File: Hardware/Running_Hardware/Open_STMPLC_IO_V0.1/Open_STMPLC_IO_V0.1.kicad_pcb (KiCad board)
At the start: 4 copper layers, 168.8 x 90 mm, 555 parts, among them J1 Screw_Terminal_01x10, J2 Screw_Terminal_01x06, J3 Screw_Terminal_01x04, J33 Screw_Terminal_01x02, J34 Screw_Terminal_01x02, J35 Screw_Terminal_01x03, J36 Screw_Terminal_01x03, J37 Screw_Terminal_01x03, J38 Screw_Terminal_01x03, J39 10144517-041802LF, J4 Screw_Terminal_01x02, J40 Screw_Terminal_01x04, J41 10144517-041802LF, J42 10144517-041802LF, J43 Screw_Terminal_01x02, J5 Screw_Terminal_01x04, J6 Screw_Terminal_01x04, J7 Screw_Terminal_01x04, J8 Screw_Terminal_01x04, J9 DE9_Pins, Q1 2N7002K, Q2 2N7002K, Q3 2N7002K, Q4 2N7002K, Q5 AOD407, Q6 AOD407, Q7 MMBT5401, U1 TPS1H200A, U10 MAX31865xTP, U11 MAX31856, U12 6N137, U13 TPS1H200A, U14 TPS26600PWP, U15 NVTFS5124PLTAG, U16 TPS26600PWP, U17 NVTFS5124PLTAG, U18 TPS26600PWP, U19 NVTFS5124PLTAG, U2 TPS1H200A, U20 6N137, U21 6N137, U22 6N137, U23 6N137, U24 6N137, U25 6N137, U26 6N137, U27 6N137, U28 6N137, U29 6N137, U3 TPS1H200A, U30 6N137, U37 XTR305, U38 XTR305, U39 AD4111, U4 TPS1H200A, U40 REF3025, U41 MAX31865xTP, U5 TPS1H200A, U6 TPS1H200A, U7 TPS26600PWP, U8 NVTFS5124PLTAG, U9 TPS1H200A, Y2 16MHz

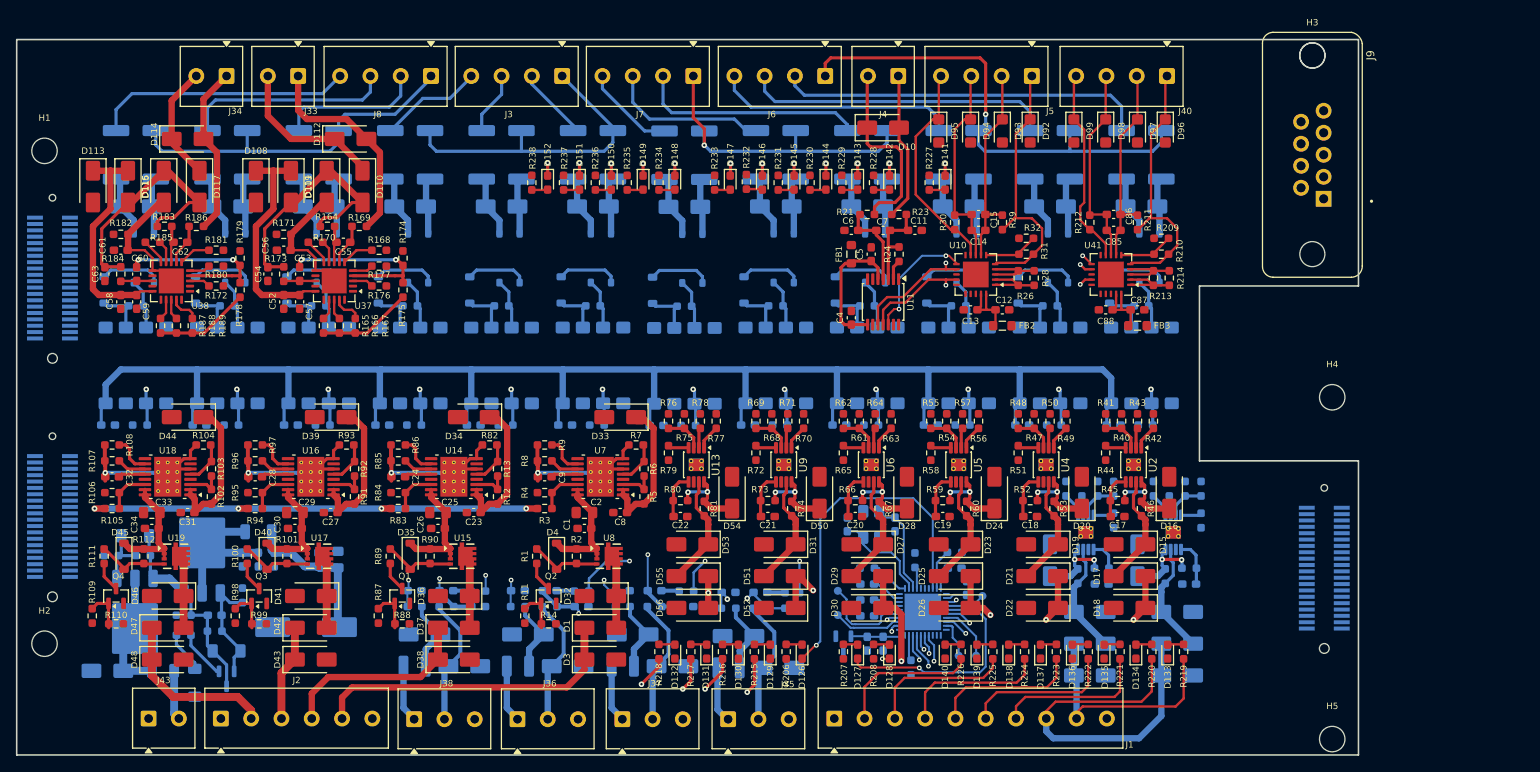
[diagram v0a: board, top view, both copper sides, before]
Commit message: Pin mapping IO connector
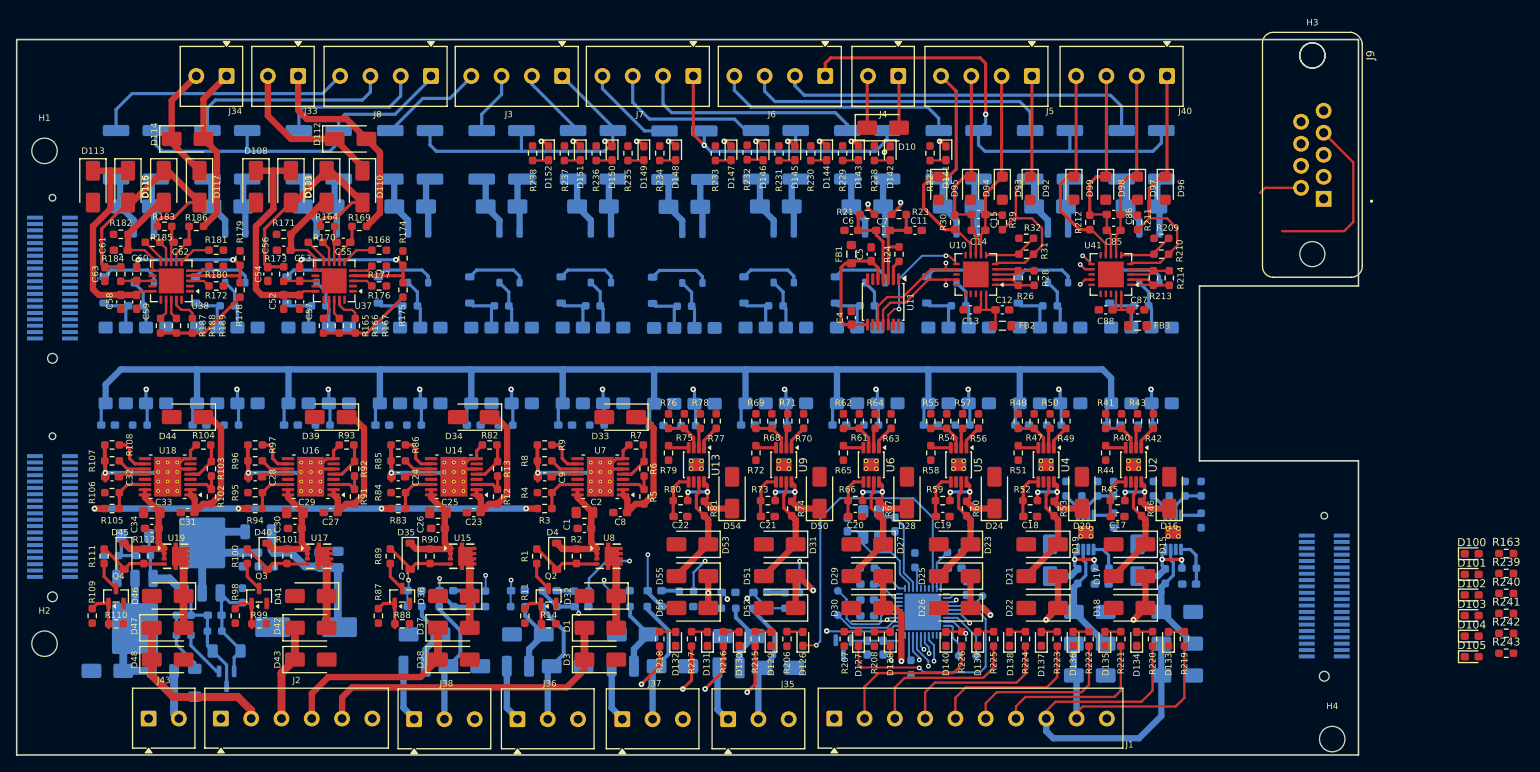
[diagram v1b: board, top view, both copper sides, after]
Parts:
- removed H5: MountingHole, MountingHole:MountingHole_3.2mm_M3
- added D100: LED, LED_SMD:LED_0603_1608Metric_Pad1.05x0.95mm_HandSolder, F.Cu at (231.0, 124.7)
- added D101: LED, LED_SMD:LED_0603_1608Metric_Pad1.05x0.95mm_HandSolder, F.Cu at (231.0, 127.3)
- added D102: LED, LED_SMD:LED_0603_1608Metric_Pad1.05x0.95mm_HandSolder, F.Cu at (231.0, 129.9)
- added D103: LED, LED_SMD:LED_0603_1608Metric_Pad1.05x0.95mm_HandSolder, F.Cu at (231.0, 132.5)
- added D104: LED, LED_SMD:LED_0603_1608Metric_Pad1.05x0.95mm_HandSolder, F.Cu at (231.0, 135.1)
- added D105: LED, LED_SMD:LED_0603_1608Metric_Pad1.05x0.95mm_HandSolder, F.Cu at (231.0, 137.6)
- added R163: 470R, Resistor_SMD:R_0603_1608Metric_Pad0.98x0.95mm_HandSolder, F.Cu at (235.4, 124.7)
- added R239: 470R, Resistor_SMD:R_0603_1608Metric_Pad0.98x0.95mm_HandSolder, F.Cu at (235.4, 127.2)
- added R240: 470R, Resistor_SMD:R_0603_1608Metric_Pad0.98x0.95mm_HandSolder, F.Cu at (235.4, 129.7)
- added R241: 470R, Resistor_SMD:R_0603_1608Metric_Pad0.98x0.95mm_HandSolder, F.Cu at (235.4, 132.2)
- added R242: 470R, Resistor_SMD:R_0603_1608Metric_Pad0.98x0.95mm_HandSolder, F.Cu at (235.4, 134.7)
- added R243: 470R, Resistor_SMD:R_0603_1608Metric_Pad0.98x0.95mm_HandSolder, F.Cu at (235.4, 137.2)
- moved H4 43.0 mm to (213.5, 148.0)
- moved D92 7.20 mm to (175.5, 78.7)
- moved D93 7.20 mm to (172.0, 78.7)
- moved D94 7.20 mm to (168.0, 78.7)
- moved D95 7.20 mm to (164.0, 78.7)
- moved D96 7.20 mm to (192.5, 78.7)
- moved D97 7.20 mm to (189.0, 78.7)
- moved D98 7.20 mm to (185.0, 78.7)
- moved D99 7.20 mm to (181.0, 78.7)
- moved D147 3.70 mm to (137.9, 74.3)
- moved D141 3.70 mm to (164.9, 74.3)
- moved D142 3.70 mm to (157.9, 74.3)
- moved D143 3.70 mm to (153.9, 74.3)
- moved D144 3.70 mm to (149.9, 74.3)
- moved D145 3.70 mm to (145.9, 74.3)
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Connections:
- J39 pad 1: unconnected-(J39-Pin_1-Pad1) -> GND
- J39 pad 2: unconnected-(J39-Pin_2-Pad2) -> GND
- J39 pad 39: unconnected-(J39-Pin_39-Pad39) -> GND
- J39 pad 40: unconnected-(J39-Pin_40-Pad40) -> GND
- J41 pad 1: unconnected-(J41-Pin_1-Pad1) -> GND
- J41 pad 2: unconnected-(J41-Pin_2-Pad2) -> GND
- J41 pad 3: unconnected-(J41-Pin_3-Pad3) -> +24V
- J41 pad 39: unconnected-(J41-Pin_39-Pad39) -> GND
- J41 pad 4: unconnected-(J41-Pin_4-Pad4) -> +3V3
- J41 pad 40: unconnected-(J41-Pin_40-Pad40) -> GND
- J41 pad 5: unconnected-(J41-Pin_5-Pad5) -> +24V
- J41 pad 6: unconnected-(J41-Pin_6-Pad6) -> +3V3
- J41 pad 7: unconnected-(J41-Pin_7-Pad7) -> +24V
- J41 pad 8: unconnected-(J41-Pin_8-Pad8) -> +3V3
- J42 pad 1: unconnected-(J42-Pin_1-Pad1) -> GND
- J42 pad 2: unconnected-(J42-Pin_2-Pad2) -> GND
- J42 pad 33: unconnected-(J42-Pin_33-Pad33) -> /B2B_Connector/AB-
- J42 pad 34: unconnected-(J42-Pin_34-Pad34) -> /B2B_Connector/YZ+
- J42 pad 35: unconnected-(J42-Pin_35-Pad35) -> /B2B_Connector/AB+
- J42 pad 36: unconnected-(J42-Pin_36-Pad36) -> /B2B_Connector/YZ-
- J42 pad 37: unconnected-(J42-Pin_37-Pad37) -> /B2B_Connector/3V3_ISO
- J42 pad 38: unconnected-(J42-Pin_38-Pad38) -> GND_MODBUS
- J42 pad 39: unconnected-(J42-Pin_39-Pad39) -> GND
- J42 pad 40: unconnected-(J42-Pin_40-Pad40) -> GND
- J9 pad 1: unconnected-(J9-Pad1) -> GND_MODBUS
- J9 pad 2: unconnected-(J9-Pad2) -> /B2B_Connector/AB-
- J9 pad 3: unconnected-(J9-Pad3) -> /B2B_Connector/AB+
- J9 pad 4: unconnected-(J9-Pad4) -> /B2B_Connector/YZ-
- J9 pad 5: unconnected-(J9-Pad5) -> GND_MODBUS
- J9 pad 6: unconnected-(J9-Pad6) -> /B2B_Connector/YZ+
- J9 pad 9: unconnected-(J9-Pad9) -> /B2B_Connector/3V3_ISO
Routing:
- net /B2B_Connector/YZ-: track 0.00 -> 22.2 mm
- net Net-(D10-A2): track 18.7 -> 24.5 mm, vias 0 -> 1
- net /B2B_Connector/YZ+: track 0.00 -> 5.45 mm
- net /B2B_Connector/DIG_IN_4: track 40.0 -> 42.8 mm
- net /B2B_Connector/DIG_IN_3: track 46.9 -> 49.7 mm
- net Net-(D91-K): track 5.20 -> 7.71 mm
- net /ANALOG_IN/VIN2: track 50.6 -> 53.1 mm
- net /B2B_Connector/DIG_IN_1: track 61.6 -> 63.9 mm
- net Net-(D99-A1): track 24.9 -> 27.0 mm
- net /B2B_Connector/DIG_IN_5: track 35.0 -> 37.1 mm
- net Net-(D95-A1): track 27.6 -> 29.5 mm
- net /B2B_Connector/DIG_OUT_TERMINAL_7: track 72.3 -> 73.9 mm
- net /B2B_Connector/DIG_OUT_TERMINAL_5: track 40.5 -> 42.1 mm
- net /B2B_Connector/DIG_OUT_TERMINAL_3: track 46.9 -> 48.5 mm
- net /B2B_Connector/DIG_OUT_TERMINAL_2: track 46.0 -> 47.7 mm
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
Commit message: IO board layout
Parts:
- moved R243 81.9 mm to (183.0, 74.3), turned to 90 degrees
- moved D105 78.4 mm to (184.9, 74.3), turned to -90 degrees
- moved R242 77.4 mm to (186.9, 74.3), turned to 90 degrees
- moved D104 73.9 mm to (188.9, 74.3), turned to -90 degrees
- moved R241 72.9 mm to (191.0, 74.3), turned to 90 degrees
- moved D103 69.6 mm to (192.9, 74.3), turned to -90 degrees
- moved R240 32.0 mm to (205.9, 142.0)
- moved R239 31.1 mm to (205.9, 136.9)
- moved R163 30.4 mm to (205.9, 132.0)
- moved D102 27.1 mm to (205.9, 139.9), turned to 180 degrees
- moved D101 26.2 mm to (205.9, 134.8), turned to 180 degrees
- moved D100 25.7 mm to (205.9, 129.9), turned to 180 degrees
- moved C83 2.83 mm to (150.5, 123.0), turned to -90 degrees
- moved Y2 2.24 mm to (154.5, 123.0), turned to 180 degrees
- moved C84 2.00 mm to (158.5, 123.0), turned to 90 degrees
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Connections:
- D100 pad 1: /B2B_Connector/POWER_LED -> GND
- D103 pad 1: /B2B_Connector/Ethernet_Link_LED -> /B2B_Connector/NET_STATUS_LED
- D104 pad 1: /B2B_Connector/Ethernet_Activity_LED -> /B2B_Connector/NET_MODE_LED
- D105 pad 1: /B2B_Connector/Internet_Status_LED -> /B2B_Connector/GSM_STATUS_LED
- J39 pad 10: unconnected-(J39-Pin_10-Pad10) -> /ANALOG_OUT/AOUT_~{OD}_2
- J39 pad 11: unconnected-(J39-Pin_11-Pad11) -> /ANALOG_OUT/AOUT_EFOT_1
- J39 pad 12: unconnected-(J39-Pin_12-Pad12) -> /ANALOG_OUT/AOUT_EFOT_2
- J39 pad 13: unconnected-(J39-Pin_13-Pad13) -> /ANALOG_OUT/AOUT_EFLD_1
- J39 pad 14: unconnected-(J39-Pin_14-Pad14) -> /ANALOG_OUT/AOUT_EFLD_2
- J39 pad 15: unconnected-(J39-Pin_15-Pad15) -> /ANALOG_OUT/AOUT_EFCM_1
- J39 pad 16: unconnected-(J39-Pin_16-Pad16) -> /ANALOG_OUT/AOUT_EFCM_2
- J39 pad 17: unconnected-(J39-Pin_17-Pad17) -> /B2B_Connector/TEMP_MISO
- J39 pad 18: unconnected-(J39-Pin_18-Pad18) -> /B2B_Connector/THRM_~{CS}
- J39 pad 19: unconnected-(J39-Pin_19-Pad19) -> /B2B_Connector/RTD_~{CS}_1
- J39 pad 20: unconnected-(J39-Pin_20-Pad20) -> /B2B_Connector/THRM_~{FAULT}
- J39 pad 21: unconnected-(J39-Pin_21-Pad21) -> /B2B_Connector/RTD_~{CS}_2
- J39 pad 22: unconnected-(J39-Pin_22-Pad22) -> /B2B_Connector/RTD_~{DRDY}_1
- J39 pad 23: unconnected-(J39-Pin_23-Pad23) -> /B2B_Connector/TEMP_SCLK
- J39 pad 24: unconnected-(J39-Pin_24-Pad24) -> /B2B_Connector/THRM_~{DRDY}
- J39 pad 25: unconnected-(J39-Pin_25-Pad25) -> /B2B_Connector/TEMP_MOSI
- J39 pad 26: unconnected-(J39-Pin_26-Pad26) -> /B2B_Connector/RTD_~{DRDY}_2
- J39 pad 27: unconnected-(J39-Pin_27-Pad27) -> /B2B_Connector/DIG_IN_6
- J39 pad 28: unconnected-(J39-Pin_28-Pad28) -> /B2B_Connector/GSM_STATUS_LED
- J39 pad 29: unconnected-(J39-Pin_29-Pad29) -> /B2B_Connector/DIG_IN_5
- J39 pad 3: unconnected-(J39-Pin_3-Pad3) -> /ANALOG_OUT/AOUT_VIN_1
- J39 pad 30: unconnected-(J39-Pin_30-Pad30) -> /B2B_Connector/NET_MODE_LED
- J39 pad 31: unconnected-(J39-Pin_31-Pad31) -> /B2B_Connector/DIG_IN_4
- J39 pad 32: unconnected-(J39-Pin_32-Pad32) -> /B2B_Connector/NET_STATUS_LED
- J39 pad 33: unconnected-(J39-Pin_33-Pad33) -> /B2B_Connector/DIG_IN_3
- J39 pad 35: unconnected-(J39-Pin_35-Pad35) -> /B2B_Connector/DIG_IN_2
- J39 pad 37: unconnected-(J39-Pin_37-Pad37) -> /B2B_Connector/DIG_IN_1
- J39 pad 4: unconnected-(J39-Pin_4-Pad4) -> /ANALOG_OUT/AOUT_VIN_2
- J39 pad 5: unconnected-(J39-Pin_5-Pad5) -> /ANALOG_OUT/AOUT_M1_1
- J39 pad 6: unconnected-(J39-Pin_6-Pad6) -> /ANALOG_OUT/AOUT_M1_2
- J39 pad 7: unconnected-(J39-Pin_7-Pad7) -> /ANALOG_OUT/AOUT_M2_1
- J39 pad 8: unconnected-(J39-Pin_8-Pad8) -> /ANALOG_OUT/AOUT_M2_2
- J39 pad 9: unconnected-(J39-Pin_9-Pad9) -> /ANALOG_OUT/AOUT_~{OD}_1
- J41 pad 10: unconnected-(J41-Pin_10-Pad10) -> /B2B_Connector/DIG_HS_IMON_2
- J41 pad 11: unconnected-(J41-Pin_11-Pad11) -> /B2B_Connector/DIG_HS_~{FAULT}_1
- J41 pad 12: unconnected-(J41-Pin_12-Pad12) -> /B2B_Connector/DIG_HS_~{FAULT}_2
- J41 pad 13: unconnected-(J41-Pin_13-Pad13) -> /B2B_Connector/DIG_HS_OUT_1
- J41 pad 14: unconnected-(J41-Pin_14-Pad14) -> /B2B_Connector/DIG_HS_OUT_2
- J41 pad 15: unconnected-(J41-Pin_15-Pad15) -> GND
- J41 pad 16: unconnected-(J41-Pin_16-Pad16) -> GND
- J41 pad 17: unconnected-(J41-Pin_17-Pad17) -> /B2B_Connector/DIG_HS_OUT_3
- J41 pad 18: unconnected-(J41-Pin_18-Pad18) -> /B2B_Connector/DIG_HS_OUT_4
- J41 pad 19: unconnected-(J41-Pin_19-Pad19) -> /B2B_Connector/DIG_HS_~{SHDN}_3
- J41 pad 20: unconnected-(J41-Pin_20-Pad20) -> /B2B_Connector/DIG_HS_~{SHDN}_4
- J41 pad 21: unconnected-(J41-Pin_21-Pad21) -> /B2B_Connector/DIG_HS_~{FAULT}_3
- J41 pad 22: unconnected-(J41-Pin_22-Pad22) -> /B2B_Connector/DIG_HS_IMON_4
- J41 pad 23: unconnected-(J41-Pin_23-Pad23) -> /B2B_Connector/DIG_HS_IMON_3
- J41 pad 24: unconnected-(J41-Pin_24-Pad24) -> /B2B_Connector/DIG_HS_~{FAULT}_4
- J41 pad 25: unconnected-(J41-Pin_25-Pad25) -> GND
- J41 pad 26: unconnected-(J41-Pin_26-Pad26) -> GND
- J41 pad 27: unconnected-(J41-Pin_27-Pad27) -> /ANALOG_IN/ANALOG_IN_DOUT
- J41 pad 28: unconnected-(J41-Pin_28-Pad28) -> /ANALOG_IN/ANALOG_IN_CS
- J41 pad 29: unconnected-(J41-Pin_29-Pad29) -> /ANALOG_IN/ANALOG_IN_DIN
- J41 pad 30: unconnected-(J41-Pin_30-Pad30) -> /ANALOG_IN/ANALOG_IN_ERROR
- J41 pad 31: unconnected-(J41-Pin_31-Pad31) -> /ANALOG_IN/ANALOG_IN_SCLK
- J41 pad 32: unconnected-(J41-Pin_32-Pad32) -> GND
- J41 pad 33: unconnected-(J41-Pin_33-Pad33) -> /B2B_Connector/DIG_IN_10
- J41 pad 34: unconnected-(J41-Pin_34-Pad34) -> /B2B_Connector/DIG_IN_7
- J41 pad 35: unconnected-(J41-Pin_35-Pad35) -> /B2B_Connector/DIG_IN_11
- J41 pad 36: unconnected-(J41-Pin_36-Pad36) -> /B2B_Connector/DIG_IN_8
- J41 pad 37: unconnected-(J41-Pin_37-Pad37) -> /B2B_Connector/DIG_IN_12
- J41 pad 38: unconnected-(J41-Pin_38-Pad38) -> /B2B_Connector/DIG_IN_9
- J41 pad 7: +24V -> /B2B_Connector/DIG_HS_~{SHDN}_1
- J41 pad 8: +3V3 -> /B2B_Connector/DIG_HS_~{SHDN}_2
- J41 pad 9: unconnected-(J41-Pin_9-Pad9) -> /B2B_Connector/DIG_HS_IMON_1
- J42 pad 10: unconnected-(J42-Pin_10-Pad10) -> /B2B_Connector/DIG_OUT_~{FAULT}_5
- J42 pad 11: unconnected-(J42-Pin_11-Pad11) -> /B2B_Connector/DIG_OUT_DIAG_6
- J42 pad 12: unconnected-(J42-Pin_12-Pad12) -> /B2B_Connector/DIG_OUT_DIAG_5
- J42 pad 13: unconnected-(J42-Pin_13-Pad13) -> /B2B_Connector/DIG_OUT_6
- J42 pad 14: unconnected-(J42-Pin_14-Pad14) -> /B2B_Connector/DIG_OUT_5
- J42 pad 15: unconnected-(J42-Pin_15-Pad15) -> /B2B_Connector/RUN_LED
- J42 pad 16: unconnected-(J42-Pin_16-Pad16) -> /B2B_Connector/FAULT_LED
- J42 pad 17: unconnected-(J42-Pin_17-Pad17) -> /B2B_Connector/DIG_OUT_~{FAULT}_4
- J42 pad 18: unconnected-(J42-Pin_18-Pad18) -> /B2B_Connector/DIG_OUT_~{FAULT}_3
- J42 pad 19: unconnected-(J42-Pin_19-Pad19) -> /B2B_Connector/DIG_OUT_DIAG_4
- J42 pad 20: unconnected-(J42-Pin_20-Pad20) -> /B2B_Connector/DIG_OUT_DIAG_3
- J42 pad 21: unconnected-(J42-Pin_21-Pad21) -> /B2B_Connector/DIG_OUT_4
- J42 pad 22: unconnected-(J42-Pin_22-Pad22) -> /B2B_Connector/DIG_OUT_3
- J42 pad 23: unconnected-(J42-Pin_23-Pad23) -> /B2B_Connector/DIG_OUT_2
- J42 pad 24: unconnected-(J42-Pin_24-Pad24) -> /B2B_Connector/DIG_OUT_1
- J42 pad 25: unconnected-(J42-Pin_25-Pad25) -> /B2B_Connector/DIG_OUT_DIAG_2
- J42 pad 26: unconnected-(J42-Pin_26-Pad26) -> /B2B_Connector/DIG_OUT_DIAG_1
- J42 pad 27: unconnected-(J42-Pin_27-Pad27) -> /B2B_Connector/DIG_OUT_~{FAULT}_2
- J42 pad 28: unconnected-(J42-Pin_28-Pad28) -> /B2B_Connector/DIG_OUT_~{FAULT}_1
- J42 pad 29: unconnected-(J42-Pin_29-Pad29) -> /B2B_Connector/3V3_ISO
- J42 pad 3: unconnected-(J42-Pin_3-Pad3) -> /B2B_Connector/DIG_OUT_~{FAULT}_7
- J42 pad 30: unconnected-(J42-Pin_30-Pad30) -> GND
- J42 pad 31: unconnected-(J42-Pin_31-Pad31) -> GND_MODBUS
- J42 pad 32: unconnected-(J42-Pin_32-Pad32) -> GND_MODBUS
- J42 pad 33: /B2B_Connector/AB- -> /B2B_Connector/YZ-
- J42 pad 34: /B2B_Connector/YZ+ -> /B2B_Connector/AB-
- J42 pad 35: /B2B_Connector/AB+ -> /B2B_Connector/YZ+
- J42 pad 36: /B2B_Connector/YZ- -> /B2B_Connector/AB+
- J42 pad 37: /B2B_Connector/3V3_ISO -> GND_MODBUS
- J42 pad 4: unconnected-(J42-Pin_4-Pad4) -> /B2B_Connector/DIG_OUT_~{FAULT}_8
- J42 pad 5: unconnected-(J42-Pin_5-Pad5) -> /B2B_Connector/DIG_OUT_DIAG_7
- J42 pad 6: unconnected-(J42-Pin_6-Pad6) -> /B2B_Connector/DIG_OUT_DIAG_8
- J42 pad 7: unconnected-(J42-Pin_7-Pad7) -> /B2B_Connector/DIG_OUT_7
- J42 pad 8: unconnected-(J42-Pin_8-Pad8) -> /B2B_Connector/DIG_OUT_8
- J42 pad 9: unconnected-(J42-Pin_9-Pad9) -> /B2B_Connector/DIG_OUT_~{FAULT}_6
- R17 pad 1: /DIG_OUT/DIG_OUT_~{FAULT}_1 -> /B2B_Connector/DIG_OUT_~{FAULT}_1
- R19 pad 1: /B2B_Connector/DIG_OUT_DIAG_1 -> /B2B_Connector/DIG_OUT_1
- R20 pad 1: /B2B_Connector/DIG_OUT_1 -> /B2B_Connector/DIG_OUT_DIAG_1
- R33 pad 1: /DIG_OUT/DIG_OUT_~{FAULT}_2 -> /B2B_Connector/DIG_OUT_~{FAULT}_2
- R35 pad 1: /B2B_Connector/DIG_OUT_DIAG_2 -> /B2B_Connector/DIG_OUT_2
- R36 pad 1: /B2B_Connector/DIG_OUT_2 -> /B2B_Connector/DIG_OUT_DIAG_2
- R40 pad 1: /DIG_OUT/DIG_OUT_~{FAULT}_3 -> /B2B_Connector/DIG_OUT_~{FAULT}_3
- R42 pad 1: /B2B_Connector/DIG_OUT_DIAG_3 -> /B2B_Connector/DIG_OUT_3
- R43 pad 1: /B2B_Connector/DIG_OUT_3 -> /B2B_Connector/DIG_OUT_DIAG_3
- R47 pad 1: /DIG_OUT/DIG_OUT_~{FAULT}_4 -> /B2B_Connector/DIG_OUT_~{FAULT}_4
- R49 pad 1: /B2B_Connector/DIG_OUT_DIAG_4 -> /B2B_Connector/DIG_OUT_4
- R50 pad 1: /B2B_Connector/DIG_OUT_4 -> /B2B_Connector/DIG_OUT_DIAG_4
- R54 pad 1: /DIG_OUT/DIG_OUT_~{FAULT}_5 -> /B2B_Connector/DIG_OUT_~{FAULT}_5
- R56 pad 1: /B2B_Connector/DIG_OUT_DIAG_5 -> /B2B_Connector/DIG_OUT_5
- R57 pad 1: /B2B_Connector/DIG_OUT_5 -> /B2B_Connector/DIG_OUT_DIAG_5
- R61 pad 1: /DIG_OUT/DIG_OUT_~{FAULT}_6 -> /B2B_Connector/DIG_OUT_~{FAULT}_6
- R63 pad 1: /B2B_Connector/DIG_OUT_DIAG_6 -> /B2B_Connector/DIG_OUT_6
- R64 pad 1: /B2B_Connector/DIG_OUT_6 -> /B2B_Connector/DIG_OUT_DIAG_6
- R68 pad 1: /DIG_OUT/DIG_OUT_~{FAULT}_7 -> /B2B_Connector/DIG_OUT_~{FAULT}_7
- R70 pad 1: /B2B_Connector/DIG_OUT_DIAG_7 -> /B2B_Connector/DIG_OUT_7
- R71 pad 1: /B2B_Connector/DIG_OUT_7 -> /B2B_Connector/DIG_OUT_DIAG_7
- R75 pad 1: /DIG_OUT/DIG_OUT_~{FAULT}_8 -> /B2B_Connector/DIG_OUT_~{FAULT}_8
- R77 pad 1: /B2B_Connector/DIG_OUT_DIAG_8 -> /B2B_Connector/DIG_OUT_8
- R78 pad 1: /B2B_Connector/DIG_OUT_8 -> /B2B_Connector/DIG_OUT_DIAG_8
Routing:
- net /B2B_Connector/NET_STATUS_LED: track 0.00 -> 160.5 mm, vias 0 -> 2
- net /B2B_Connector/NET_MODE_LED: track 0.00 -> 156.0 mm, vias 0 -> 2
- net /B2B_Connector/GSM_STATUS_LED: track 0.00 -> 152.1 mm, vias 0 -> 2
- net /B2B_Connector/RTD_~{CS}_2: track 0.00 -> 137.3 mm, vias 0 -> 2
- net /B2B_Connector/RTD_~{DRDY}_2: track 0.00 -> 133.8 mm, vias 0 -> 2
- net /B2B_Connector/DIG_IN_1: track 63.9 -> 189.1 mm, vias 2 -> 3
- net /ANALOG_IN/ANALOG_IN_SCLK: track 0.00 -> 124.7 mm, vias 0 -> 2
- net /ANALOG_IN/ANALOG_IN_DIN: track 0.00 -> 123.6 mm, vias 0 -> 2
- net /ANALOG_IN/ANALOG_IN_CS: track 0.00 -> 120.8 mm, vias 0 -> 2
- net /ANALOG_IN/ANALOG_IN_DOUT: track 2.74 -> 123.5 mm, vias 0 -> 2
- net /B2B_Connector/RTD_~{CS}_1: track 0.00 -> 120.5 mm, vias 0 -> 2
- net /B2B_Connector/DIG_OUT_~{FAULT}_8: track 0.00 -> 120.5 mm, vias 0 -> 2
- net /B2B_Connector/DIG_IN_2: track 55.4 -> 174.8 mm, vias 2 -> 3
- net /B2B_Connector/TEMP_MISO: track 32.0 -> 151.1 mm, vias 2 -> 3
- net /B2B_Connector/DIG_OUT_DIAG_8: track 0.00 -> 119.0 mm, vias 0 -> 2
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
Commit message: Main PCB changes
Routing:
- net /B2B_Connector/3V3_ISO: track 0.00 -> 74.8 mm, vias 0 -> 1
- net /B2B_Connector/YZ-: track 89.4 -> 71.6 mm
- net Net-(D96-A1): track 21.7 -> 36.3 mm
- net Net-(D98-A1): track 13.9 -> 27.7 mm, vias 0 -> 1
- net Net-(D97-A1): track 13.8 -> 27.3 mm, vias 0 -> 1
- net GND_MODBUS: track 0.00 -> 9.62 mm, vias 0 -> 3
- net /B2B_Connector/YZ+: track 64.3 -> 71.4 mm
- net /B2B_Connector/AB-: track 75.3 -> 80.7 mm, vias 1 -> 0
- net /B2B_Connector/AB+: track 77.4 -> 80.7 mm, vias 1 -> 0
- net /B2B_Connector/GSM_STATUS_LED: track 152.1 -> 151.1 mm
- added copper zone on In1.Cu, net GND_MODBUS
- added copper zone on In2.Cu, net GND_MODBUS
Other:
- board text added: "STACK UP: JLC04161H-7628"
